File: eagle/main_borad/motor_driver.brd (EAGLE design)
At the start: 43.2 x 38.1 mm, 17 parts, among them IC1 MEGA8-AI

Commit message: PCB ver. 4.0
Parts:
- Y1: device SparkFun-FreqCtrl:HC49US -> SparkFun-FreqCtrl:HC49UP
- moved C5 9.14 mm to (14.9, 14.6), turned to 90 degrees
- moved C2 5.63 mm to (29.8, 5.40)
- moved C3 3.82 mm to (37.1, 18.1)
- moved IC1 3.82 mm to (24.8, 16.8)
- moved JP1 3.82 mm to (22.2, 30.8)
- moved JP7 3.82 mm to (40.6, 16.8)
- moved JP8 3.82 mm to (40.6, 11.1)
- moved R1 3.82 mm to (33.7, 18.1)
- moved JP2 3.82 mm to (14.9, 28.3)
- moved JP4 3.82 mm to (34.9, 9.21)
- moved JP5 3.82 mm to (32.4, 32.1)
- moved R2 3.82 mm to (34.9, 25.7)
- moved R3 3.82 mm to (29.8, 25.7)
- moved Y1 3.82 mm to (19.7, 6.67)
- moved C1 1.62 mm to (9.84, 7.94)
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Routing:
- net GND: track 37.1 -> 46.3 mm
- net N$3: track 15.6 -> 20.7 mm
- net INT1: track 5.15 -> 9.60 mm
- net VCC: track 90.1 -> 94.1 mm
- net N$2: track 17.5 -> 18.6 mm
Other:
- board size 43.2 x 38.1 mm -> 47.9 x 36.5 mm

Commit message: PCB layout 6.0
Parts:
- C5: device SparkFun-Capacitors:1206 -> SparkFun-Capacitors:0805
- moved C5 2.25 mm to (16.5, 16.2), turned to 0 degrees
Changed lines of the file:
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@@
 </class>
 </classes>
-<designrules name="default">
+<designrules name="default *">
 <description language="de">&lt;b&gt;EAGLE Design Rules&lt;/b&gt;
 &lt;p&gt;
@@
 <param name="mtCopper" value="0.035mm 0.035mm 0.035mm 0.035mm 0.035mm 0.035mm 0.035mm 0.035mm 0.035mm 0.035mm 0.035mm 0.035mm 0.035mm 0.035mm 0.035mm 0.035mm"/>
 <param name="mtIsolate" value="1.5mm 0.15mm 0.2mm 0.15mm 0.2mm 0.15mm 0.2mm 0.15mm 0.2mm 0.15mm 0.2mm 0.15mm 0.2mm 0.15mm 0.2mm"/>
-<param name="mdWireWire" value="8mil"/>
+<param name="mdWireWire" value="12mil"/>
 <param name="mdWirePad" value="8mil"/>
 <param name="mdWireVia" value="8mil"/>
@@
 <element name="C2" library="SparkFun-Capacitors" package="1206" value="220pF" x="29.845" y="5.3975" rot="R90"/>
 <element name="C3" library="SparkFun-Capacitors" package="1206" value="100nF" x="37.1475" y="18.0975" rot="R90"/>
-<element name="C5" library="SparkFun-Capacitors" package="1206" value="220nF" x="14.9225" y="14.605" rot="R90"/>
+<element name="C5" library="SparkFun-Capacitors" package="0805" value="220nF" x="16.51" y="16.1925"/>
 <element name="IC1" library="avr-7" package="TQFP32-08" value="MEGA8-AI" x="24.765" y="16.8275"/>
 <element name="JP1" library="pinhead" package="1X03" value="" x="22.225" y="30.7975" rot="R180"/>
@@
 <wire x1="23.2725" y1="14.8275" x2="22.225" y2="15.875" width="0.3048" layer="1"/>
 <wire x1="20.4724" y1="17.2275" x2="17.6975" y2="17.2275" width="0.3048" layer="1"/>
-<wire x1="17.6975" y1="17.2275" x2="17.145" y2="17.78" width="0.3048" layer="1"/>
-<wire x1="17.145" y1="17.78" x2="14.9225" y2="17.78" width="0.3048" layer="1"/>
+<wire x1="17.6975" y1="17.2275" x2="17.4625" y2="17.4625" width="0.3048" layer="1"/>
+<wire x1="17.4625" y1="17.4625" x2="17.145" y2="17.78" width="0.3048" layer="1"/>
 <wire x1="6.985" y1="16.51" x2="4.445" y2="16.51" width="0.3048" layer="1"/>
 <wire x1="29.0576" y1="14.8275" x2="30.385" y2="14.8275" width="0.3048" layer="1"/>
@@
 <wire x1="39.6875" y1="7.62" x2="39.37" y2="7.9375" width="0.3048" layer="1"/>
 <wire x1="39.37" y1="7.9375" x2="39.37" y2="9.8425" width="0.3048" layer="1"/>
-<wire x1="14.9225" y1="16.005" x2="14.9225" y2="17.78" width="0.3048" layer="1"/>
-<wire x1="14.9225" y1="17.78" x2="9.525" y2="17.78" width="0.3048" layer="1"/>
+<wire x1="17.145" y1="17.78" x2="9.525" y2="17.78" width="0.3048" layer="1"/>
 <wire x1="9.525" y1="17.78" x2="8.89" y2="18.415" width="0.3048" layer="1"/>
 <wire x1="8.89" y1="18.415" x2="8.89" y2="19.685" width="0.3048" layer="1"/>
@@
 <wire x1="12.065" y1="20.955" x2="14.9225" y2="23.8125" width="0.3048" layer="1"/>
 <wire x1="14.9225" y1="23.8125" x2="14.9225" y2="25.7175" width="0.3048" layer="1"/>
+<wire x1="17.41" y1="16.1925" x2="17.4625" y2="16.1925" width="0.3048" layer="1"/>
+<wire x1="17.4625" y1="16.1925" x2="17.4625" y2="17.4625" width="0.3048" layer="1"/>
 <wire x1="11.1125" y1="16.51" x2="9.525" y2="17.78" width="0" layer="19" extent="1-1"/>
 </signal>

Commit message: Bugs
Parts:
- removed JP6: (no value), pinhead:2X02
- C1, C2: value 220pF -> 22pF
- moved C5 3.98 mm to (18.4, 19.7)
- moved JP4 2.62 mm to (35.6, 11.7)
- moved JP5 2.62 mm to (33.0, 34.6)
- moved R2 2.62 mm to (35.6, 28.3)
- moved C2 2.62 mm to (30.5, 7.94)
- moved R3 2.62 mm to (30.5, 28.3)
- moved Y1 2.62 mm to (20.3, 9.21)
- moved C1 2.62 mm to (10.5, 10.5)
- moved JP2 2.62 mm to (15.6, 30.8)
- moved JP3 2.62 mm to (11.7, 19.1)
- moved C3 2.62 mm to (37.8, 20.6)
- moved IC1 2.62 mm to (25.4, 19.4)
- moved JP1 2.62 mm to (22.9, 33.3)
- moved JP7 2.62 mm to (41.3, 19.4)
- moved JP8 2.62 mm to (41.3, 13.7)
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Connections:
- net GND: no longer JP6.3, JP6.4
- net VCC: no longer JP6.1, JP6.2
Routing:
- net GND: track 46.3 -> 1.20 mm
- net VCC: track 93.6 -> 88.0 mm
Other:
- board size 47.9 x 36.5 mm -> 52 x 42 mm

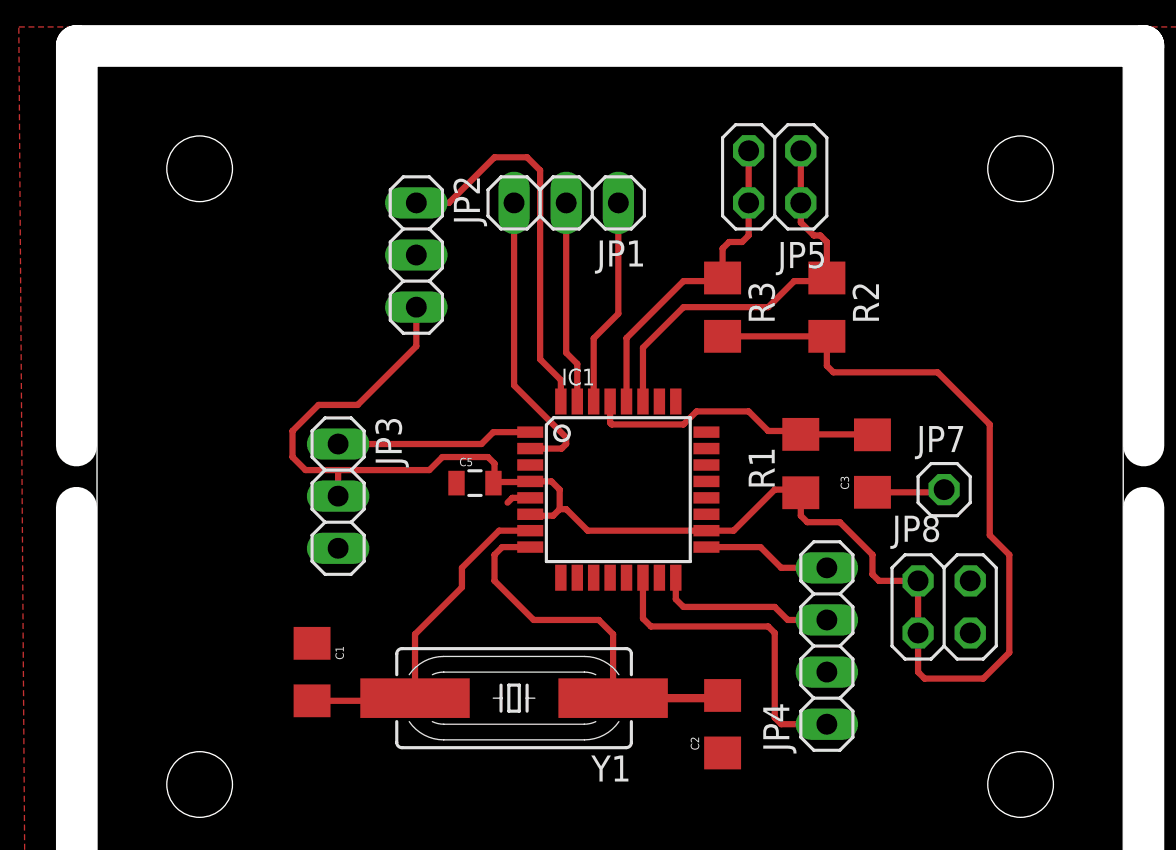
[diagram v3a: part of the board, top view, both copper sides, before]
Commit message: motor_drivers updated
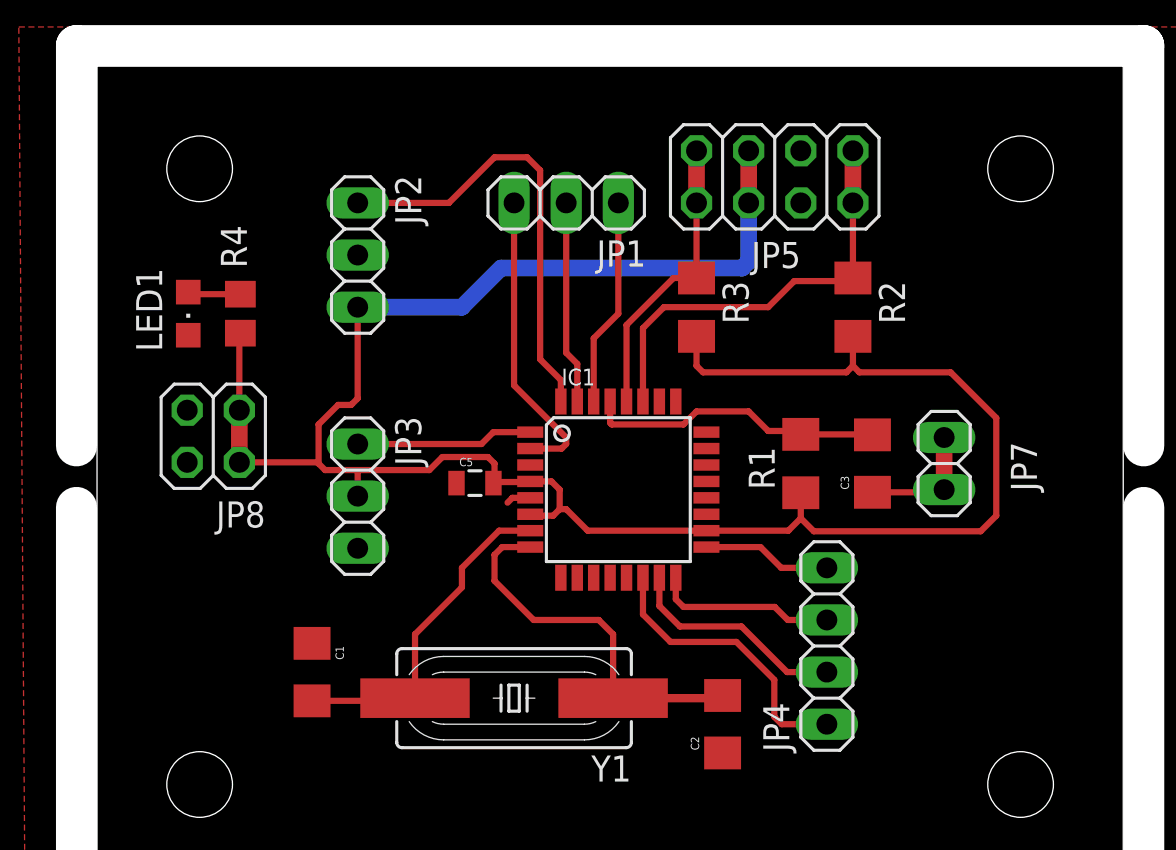
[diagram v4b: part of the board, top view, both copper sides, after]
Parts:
- added LED1: (no value), adafruit:CHIPLED_0805
- added R4: 1k, eagle-ltspice:R0805
- JP5: device pinhead:2X02 -> pinhead:2X04
- JP7: device pinhead:1X01 -> pinhead:1X02
- moved JP8 36.6 mm to (5.67, 22.0), turned to 180 degrees
- moved JP2 2.86 mm to (12.7, 30.8)
- moved JP7 1.27 mm to (41.3, 20.6), turned to 90 degrees
- moved R3 1.27 mm to (29.2, 28.3)
- moved R2 1.27 mm to (36.8, 28.3)
- moved JP3 0.95 mm to (12.7, 19.1)
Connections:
- removed net N$14: IC1.15
- new net N$11: LED1.A, R4.2
- net GND: now also JP5.3, JP5.4, LED1.C
- net N$7: now also IC1.15
- net N$9: now also JP5.7, JP5.8; no longer JP5.3, JP5.4
- net RESET: now also JP7.2
- net VCC: now also JP5.5, JP5.6, R4.1
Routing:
- net VCC: track 88.0 -> 109.1 mm
- net N$7: track 0.00 -> 10.9 mm
- net INT0: track 18.9 -> 21.8 mm
- net N$11: track 0.00 -> 2.58 mm
- net RESET: track 3.55 -> 6.09 mm
- net N$9: track 16.1 -> 14.3 mm
- net N$15: track 15.5 -> 14.0 mm
- net N$10: track 19.9 -> 21.0 mm
- net INT1: track 9.60 -> 8.65 mm

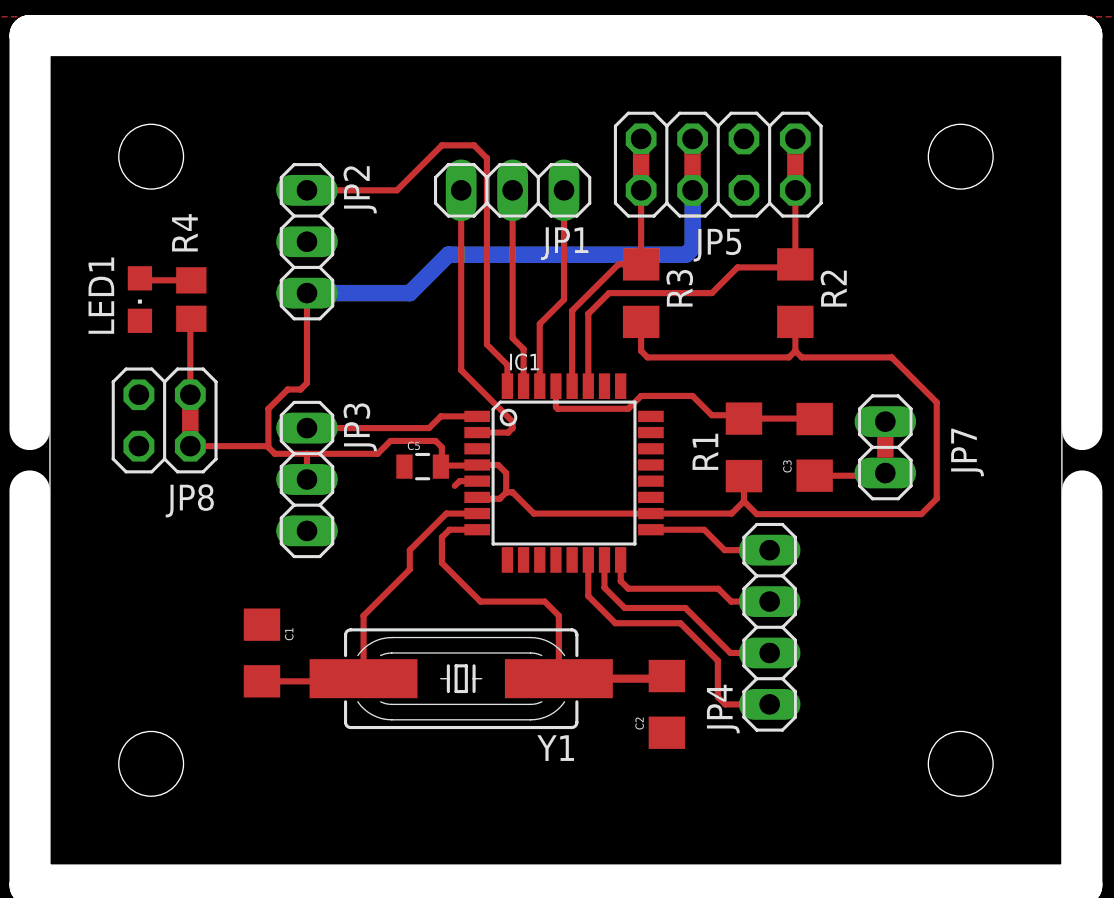
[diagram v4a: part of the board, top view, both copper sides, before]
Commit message: robot_driver updated
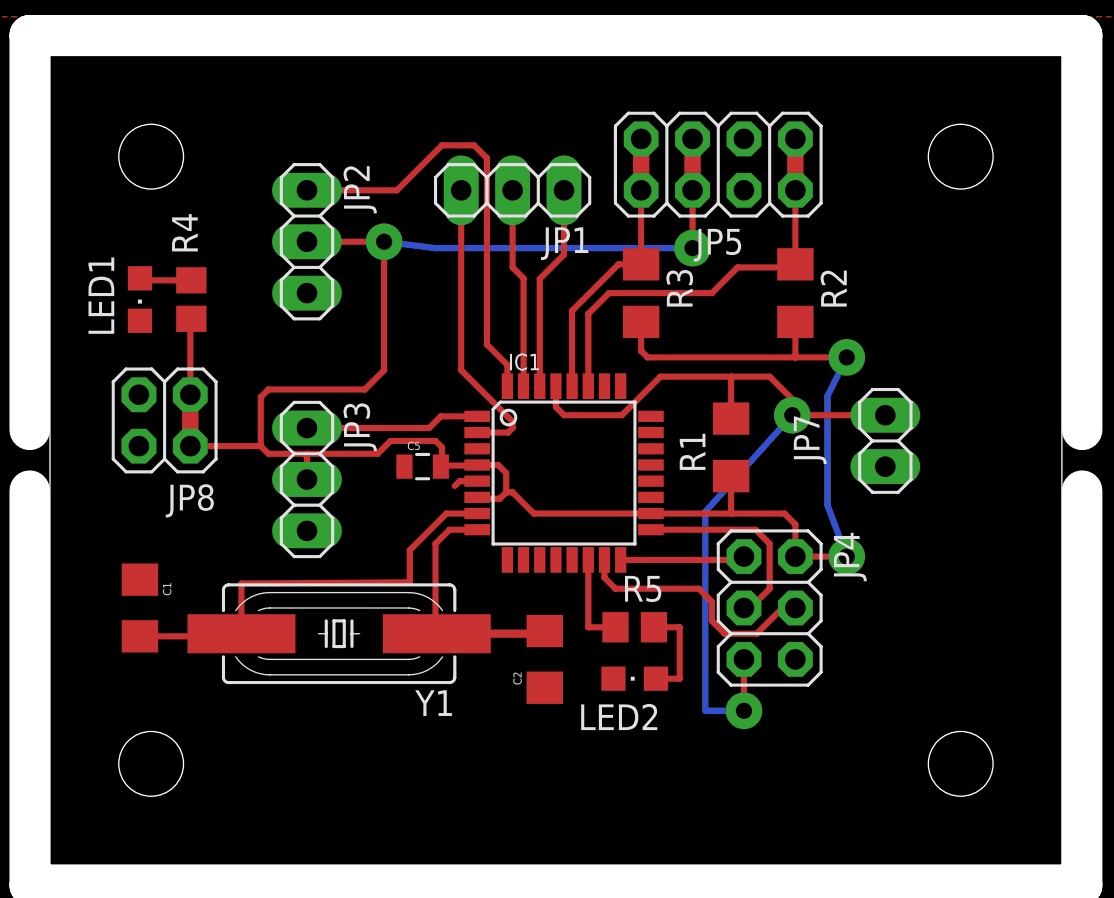
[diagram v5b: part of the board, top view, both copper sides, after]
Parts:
- removed C3: 100nF, SparkFun-Capacitors:1206
- added LED2: (no value), adafruit:CHIPLED_0805
- added R5: 1k, eagle-ltspice:R0805
- JP4: device pinhead:1X04 -> pinhead:2X03
- Y1: value (none) -> 16MHz
- moved Y1 6.43 mm to (14.3, 11.4)
- moved C1 6.43 mm to (4.45, 12.7)
- moved C2 6.43 mm to (24.4, 10.2)
- moved JP4 0.95 mm to (35.6, 12.7), turned to 270 degrees
- moved R1 0.63 mm to (33.7, 20.6)
- moved JP7 0.32 mm to (41.3, 21.0), turned to 270 degrees
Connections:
- removed net N$15: IC1.14, JP4.1
- new net N$14: LED2.A, R5.2
- net GND: now also JP2.3, JP4.6, JP7.2, LED2.C; no longer JP2.2
- net N$12: now also JP4.3; no longer JP4.4
- net N$13: now also JP4.1; no longer JP4.3
- net N$4: now also IC1.14, R5.1; no longer C3.2, IC1.29, R1.2
- net N$7: now also JP4.4; no longer JP4.2
- net RESET: now also IC1.29, JP4.5, R1.2; no longer C3.1, JP7.2
- net VCC: now also JP2.2, JP4.2; no longer JP2.3
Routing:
- net RESET: track 6.09 -> 42.3 mm, vias 0 -> 2
- net N$15: track 14.0 -> 0.00 mm
- net N$4: track 14.6 -> 4.67 mm
- net N$2: track 18.6 -> 12.3 mm
- net N$3: track 20.7 -> 25.8 mm
- net N$14: track 0.00 -> 4.98 mm
- net N$12: track 6.29 -> 10.0 mm
- net VCC: track 109.1 -> 112.5 mm, vias 0 -> 4
- net N$13: track 8.83 -> 6.26 mm
- net N$7: track 10.9 -> 12.5 mm

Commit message: NExt version motor_driver
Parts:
- R4: value 1k -> 150k
- R5: value 1k -> 22k
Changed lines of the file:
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@@
 <attribute name="VALUE" x="1.905" y="29.21" size="1.27" layer="27" rot="R270"/>
 </element>
-<element name="R4" library="eagle-ltspice" package="R0805" value="1k" x="6.985" y="27.94" smashed="yes" rot="R90">
+<element name="R4" library="eagle-ltspice" package="R0805" value="150k" x="6.985" y="27.94" smashed="yes" rot="R90">
 <attribute name="SPICEMODEL" value="NONE" x="6.985" y="27.94" size="1.778" layer="27" rot="R90" display="off"/>
 <attribute name="SPICEPREFIX" value="R" x="6.985" y="27.94" size="1.778" layer="27" rot="R90" display="off"/>
@@
 </element>
 <element name="JP4" library="pinhead" package="2X03" value="" x="35.56" y="12.7" rot="R270"/>
-<element name="R5" library="eagle-ltspice" package="R0805" value="1k" x="28.8925" y="11.7475">
+<element name="R5" library="eagle-ltspice" package="R0805" value="22k" x="28.8925" y="11.7475">
 <attribute name="SPICEMODEL" value="NONE" x="28.8925" y="11.7475" size="1.778" layer="27" display="off"/>
 <attribute name="SPICEPREFIX" value="R" x="28.8925" y="11.7475" size="1.778" layer="27" display="off"/>
